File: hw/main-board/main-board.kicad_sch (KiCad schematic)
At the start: 12 parts, among them J1 USB_C_Receptacle_USB2.0_16P, Q1 AONR21307, U1 HUSB238_xxxDD

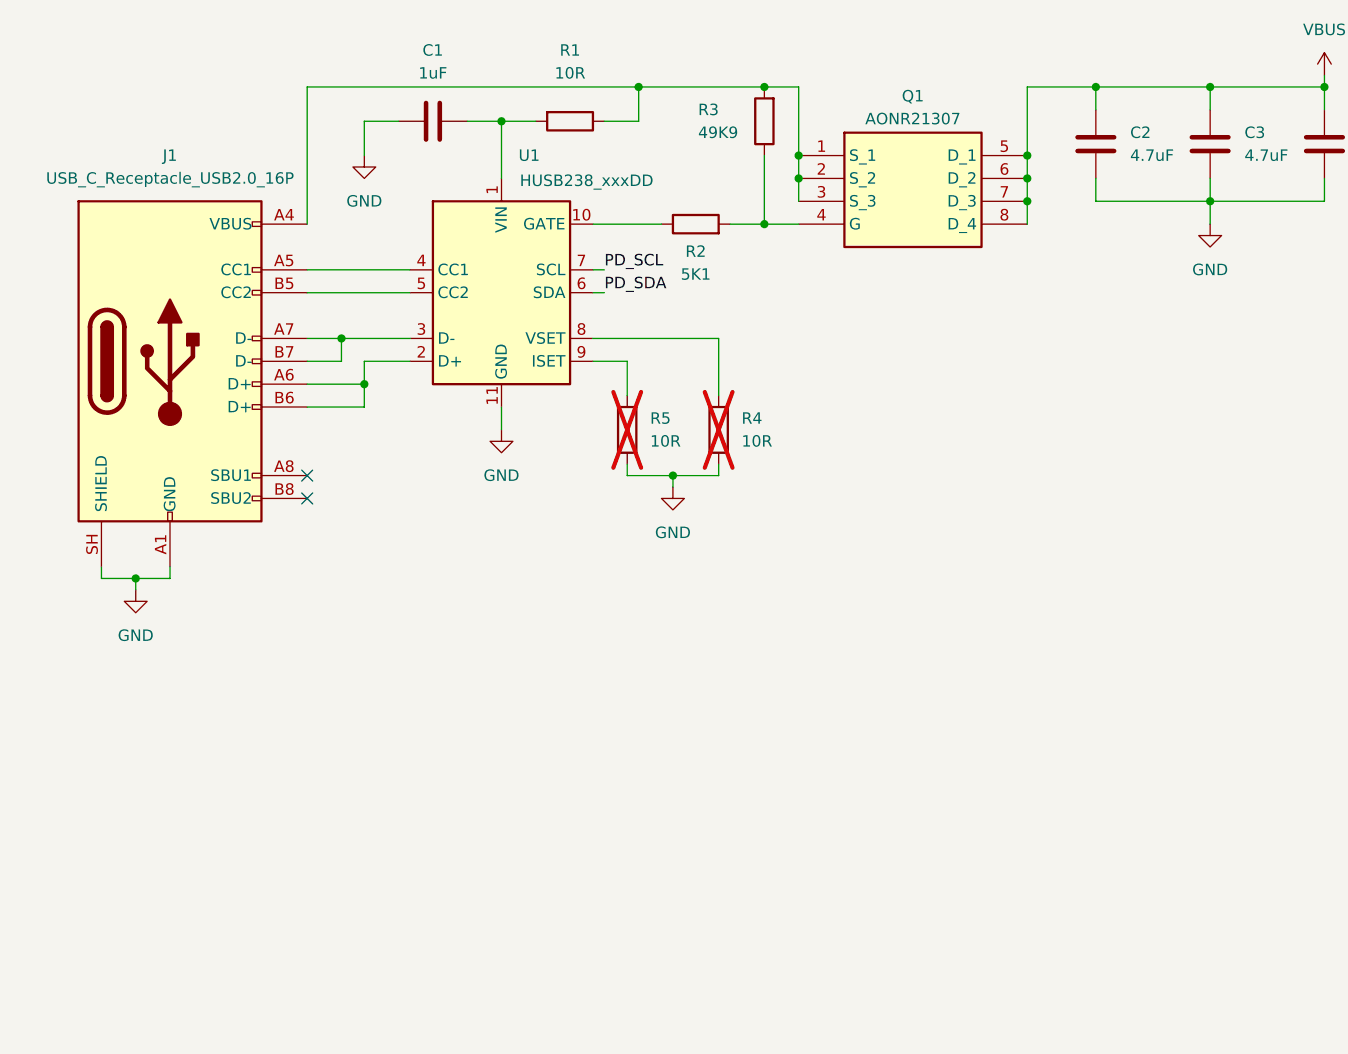
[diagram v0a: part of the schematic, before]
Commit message: Add 5V power schematic and unify components
Adds AP63205WU-based 5V buck converter schematic. Adjusts some
component choices across the board to reduce unique part count.
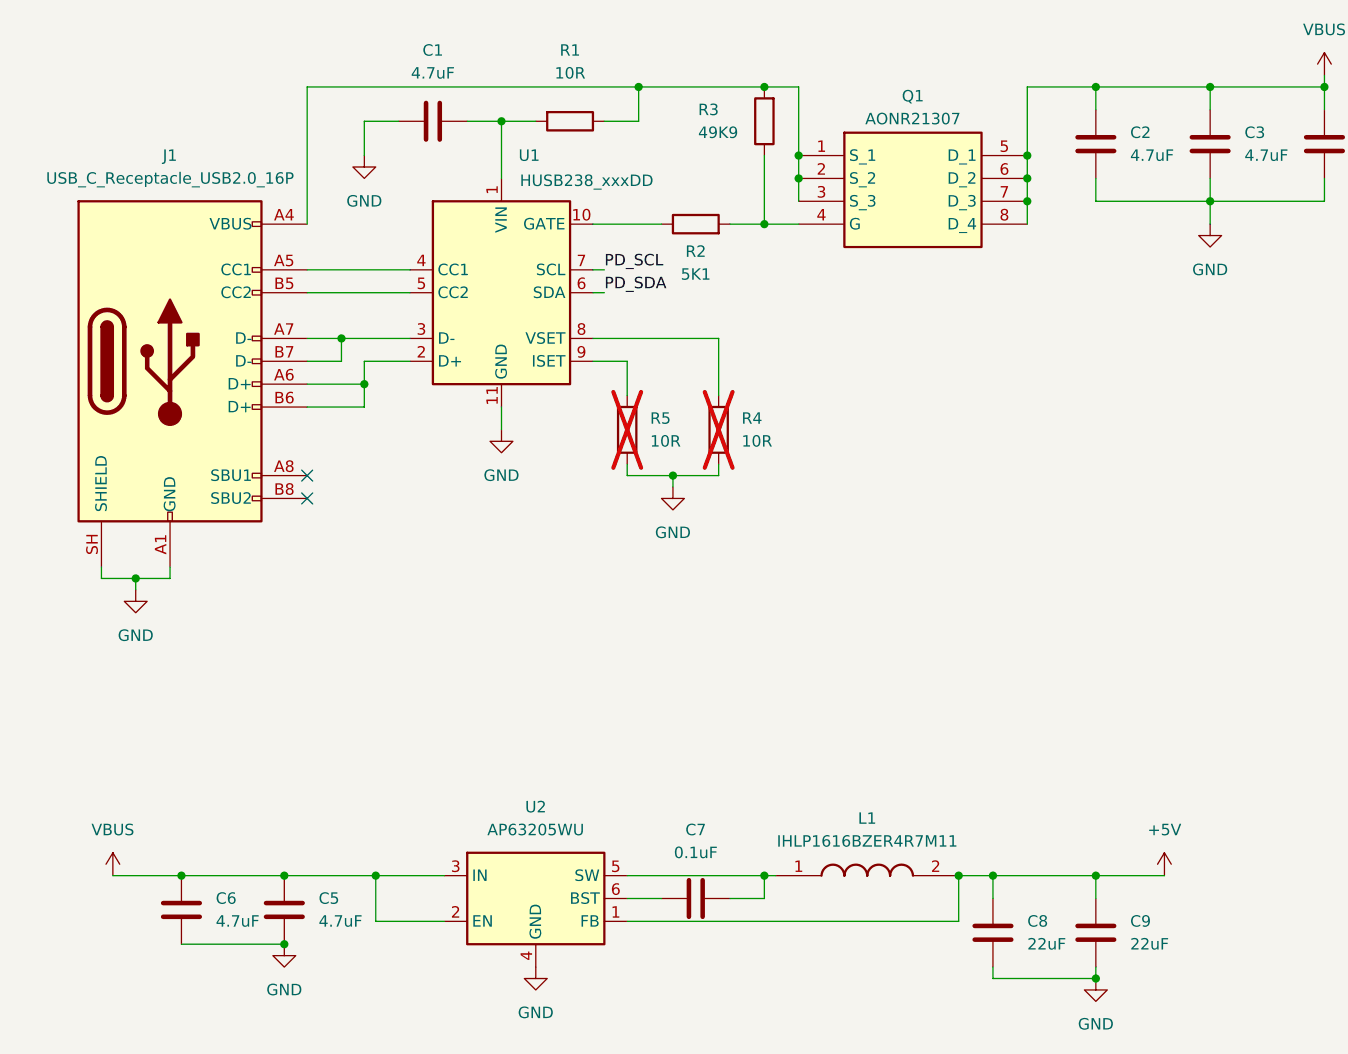
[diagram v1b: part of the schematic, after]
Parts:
- added C5, C6: 4.7uF, Capacitor_SMD:C_0805_2012Metric_Pad1.18x1.45mm_HandSolder, symbol Device:C
- added C7: 0.1uF, Capacitor_SMD:C_0603_1608Metric_Pad1.08x0.95mm_HandSolder, symbol Device:C
- added C8, C9: 22uF, Capacitor_SMD:C_0603_1608Metric_Pad1.08x0.95mm_HandSolder, symbol Device:C
- added L1: IHLP1616BZER4R7M11, INDPM4441X200N, symbol Samacsys:IHLP1616BZER4R7M11
- added U2: AP63205WU, Package_TO_SOT_SMD:TSOT-23-6_HandSoldering, symbol Regulator_Switching:AP63205WU
- C1: value 1uF -> 4.7uF
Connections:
- net GND: now also C5.2, C6.2, C8.1, C9.1, U2.4 (GND)
- net VBUS: now also C5.1, C6.1, U2.2 (EN), U2.3 (IN)
- new net: C7.2, L1.1, U2.5 (SW)
- new net: C7.1, U2.6 (BST)
- new net +5V: C8.2, C9.2, L1.2, U2.1 (FB)

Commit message: Fix SamacSys library links and correct J1 footprint
sym-lib-table pointed at the lib directory instead of the .kicad_sym
file, and there was no project fp-lib-table at all, so the SamacSys
footprints for L1/Q1 could not be resolved. Also J1 was using a
16-pin USB-C symbol paired with a 6-pin footprint that didn't have
matching pads; switched to the Palconn UTC16-G footprint, which
matches all 16 symbol pins.
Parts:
- J1: footprint Package_DFN_QFN:WDFN-10-1EP_3x3mm_P0.5mm_EP1.8x2.5mm -> Connector_USB:USB_C_Receptacle_Palconn_UTC16-G
- L1: footprint INDPM4441X200N -> Samacsys:INDPM4441X200N
- Q1: footprint DFN_3X3_EP -> Samacsys:DFN_3X3_EP
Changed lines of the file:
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@@
 			)
 		)
-		(property "Footprint" "INDPM4441X200N"
+		(property "Footprint" "Samacsys:INDPM4441X200N"
 			(at 125.73 211.76 0)
 			(hide yes)
@@
 			)
 		)
-		(property "Footprint" "Package_DFN_QFN:WDFN-10-1EP_3x3mm_P0.5mm_EP1.8x2.5mm"
+		(property "Footprint" "Connector_USB:USB_C_Receptacle_Palconn_UTC16-G"
 			(at 45.72 58.42 0)
 			(hide yes)
@@
 			)
 		)
-		(property "Footprint" "DFN_3X3_EP"
+		(property "Footprint" "Samacsys:DFN_3X3_EP"
 			(at 133.35 130.48 0)
 			(hide yes)

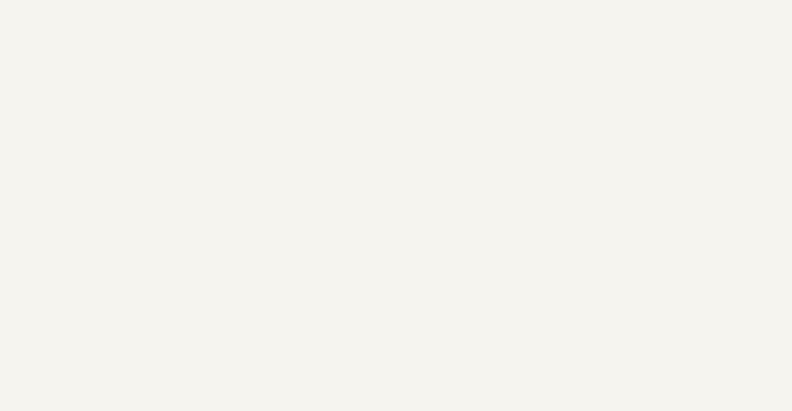
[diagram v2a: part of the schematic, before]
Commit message: Add 3.3V LDO regulator schematic (AP2112K-3.3)
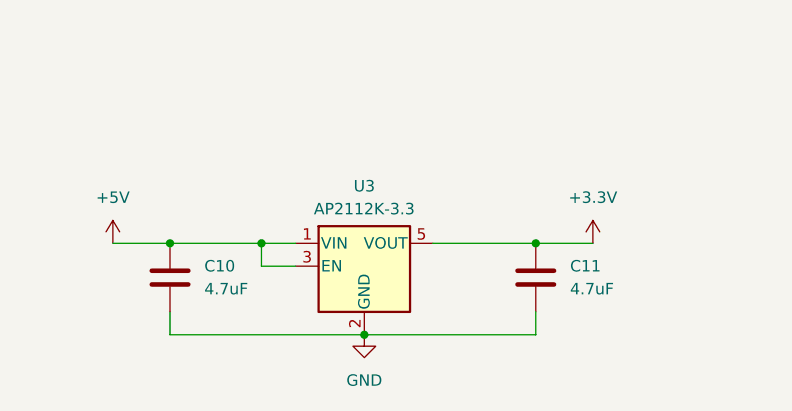
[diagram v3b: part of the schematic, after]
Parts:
- added C10, C11: 4.7uF, Capacitor_SMD:C_0603_1608Metric_Pad1.08x0.95mm_HandSolder, symbol Device:C
- added U3: AP2112K-3.3, Package_TO_SOT_SMD:SOT-23-5, symbol Regulator_Linear:AP2112K-3.3
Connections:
- net +5V: now also C10.1, U3.1 (VIN), U3.3 (EN)
- net GND: now also C10.2, C11.2, U3.2 (GND)
- new net +3.3V: C11.1, U3.5 (VOUT)

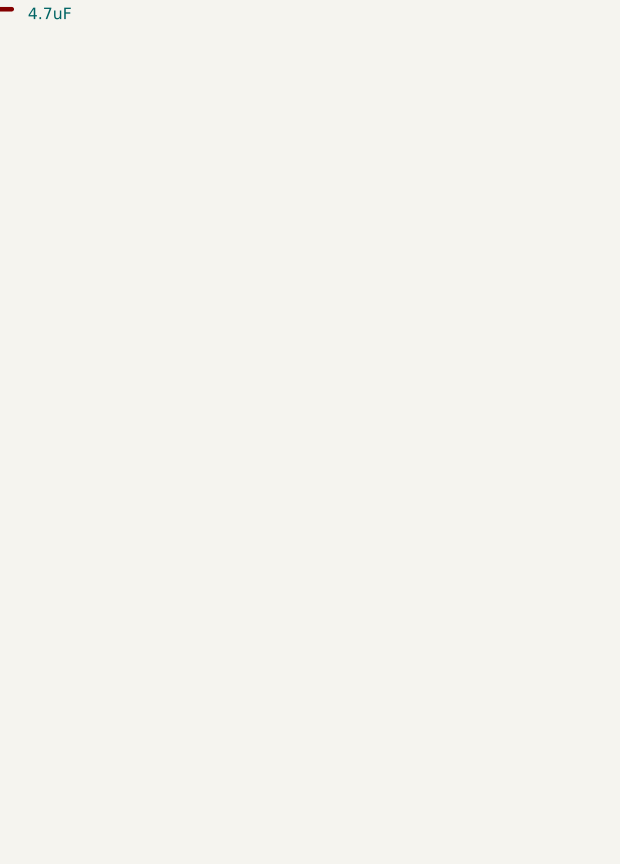
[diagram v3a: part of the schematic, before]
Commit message: Add PTR54L connector schematic with project-specific symbol and footprint library
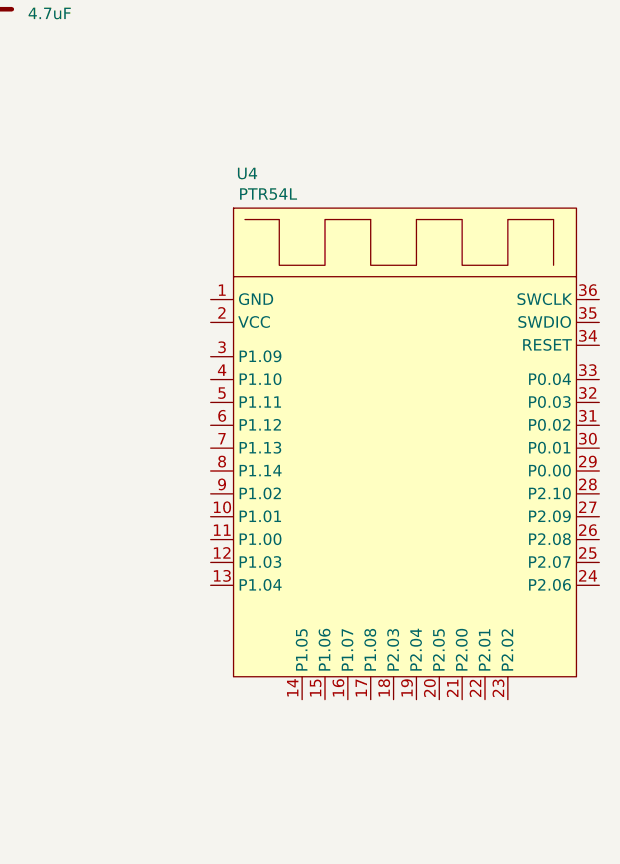
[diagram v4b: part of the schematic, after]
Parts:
- added U4: PTR54L, Project_Specific_Parts:PTR54L15, symbol Project_Specific_Parts:PTR54L
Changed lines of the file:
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@@
+	)
+	(symbol
+		(lib_id "Project_Specific_Parts:PTR54L")
+		(at 196.85 64.77 0)
+		(unit 1)
+		(body_style 1)
+		(exclude_from_sim no)
+		(in_bom yes)
+		(on_board yes)
+		(in_pos_files yes)
+		(dnp no)
+		(fields_autoplaced yes)
+		(property "Reference" "U4"
+			(at 198.374 53.34 0)
+			(show_name no)
+			(do_not_autoplace no)
+			(effects
+				(font
+					(size 1.27 1.27)
+				)
+			)
+		)
+		(property "Value" "PTR54L"
+			(at 200.66 55.626 0)
+			(show_name no)
+			(do_not_autoplace no)
+			(effects
+				(font
+					(size 1.27 1.27)
+				)
+			)
+		)
+		(property "Footprint" "Project_Specific_Parts:PTR54L15"
+			(at 196.85 64.77 0)
+			(hide yes)
+			(show_name no)
+			(do_not_autoplace no)
+			(effects
+				(font
+					(size 1.27 1.27)
+				)
+			)
+		)
+		(property "Datasheet" ""
+			(at 196.85 64.77 0)
+			(hide yes)
+			(show_name no)
+			(do_not_autoplace no)
+			(effects
+				(font
+					(size 1.27 1.27)
+				)
+			)
+		)
+		(property "Description" ""
+			(at 196.85 64.77 0)
+			(hide yes)
+			(show_name no)
+			(do_not_autoplace no)
+			(effects
+				(font
+					(size 1.27 1.27)
+				)
+			)
+		)
+		(pin "5"
+		)
+		(pin "7"
+		)
+		(pin "1"
+		)
+		(pin "14"
+		)
+		(pin "10"
+		)
+		(pin "4"
+		)
+		(pin "3"
+		)
+		(pin "11"
+		)
+		(pin "13"
+		)
+		(pin "2"
+		)
+		(pin "8"
+		)
+		(pin "9"
+		)
+		(pin "6"
+		)
+		(pin "15"
+		)
+		(pin "12"
+		)
+		(pin "33"
+		)
+		(pin "27"
+		)
+		(pin "26"
+		)
+		(pin "36"
+		)
+		(pin "35"
+		)
+		(pin "32"
+		)
+		(pin "24"
+		)
+		(pin "30"
+		)
+		(pin "17"
+		)
+		(pin "22"
+		)
+		(pin "29"
+		)
+		(pin "34"
+		)
+		(pin "18"
+		)
+		(pin "19"
+		)
+		(pin "21"
+		)
+		(pin "16"
+		)
+		(pin "23"
+		)
+		(pin "28"
+		)
+		(pin "25"
+		)
+		(pin "20"
+		)
+		(pin "31"
+		)
+		(instances
+			(project "main-board"
+				(path "/fe215afa-a228-4dbb-8560-a0753323a3f2"
+					(reference "U4")
+					(unit 1)
+				)
+			)
+		)
 	)
 	(symbol

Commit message: Add PTR54L power circuit and initial PCB outline with placed components
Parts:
- added C12: 100nF, Capacitor_SMD:C_0603_1608Metric_Pad1.08x0.95mm_HandSolder, symbol Device:C
- added C13: 22uF, Capacitor_SMD:C_0603_1608Metric_Pad1.08x0.95mm_HandSolder, symbol Device:C
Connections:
- net +3.3V: now also U4.2 (VCC), C12.2, C13.2
- net GND: now also U4.1 (GND), C12.1, C13.1

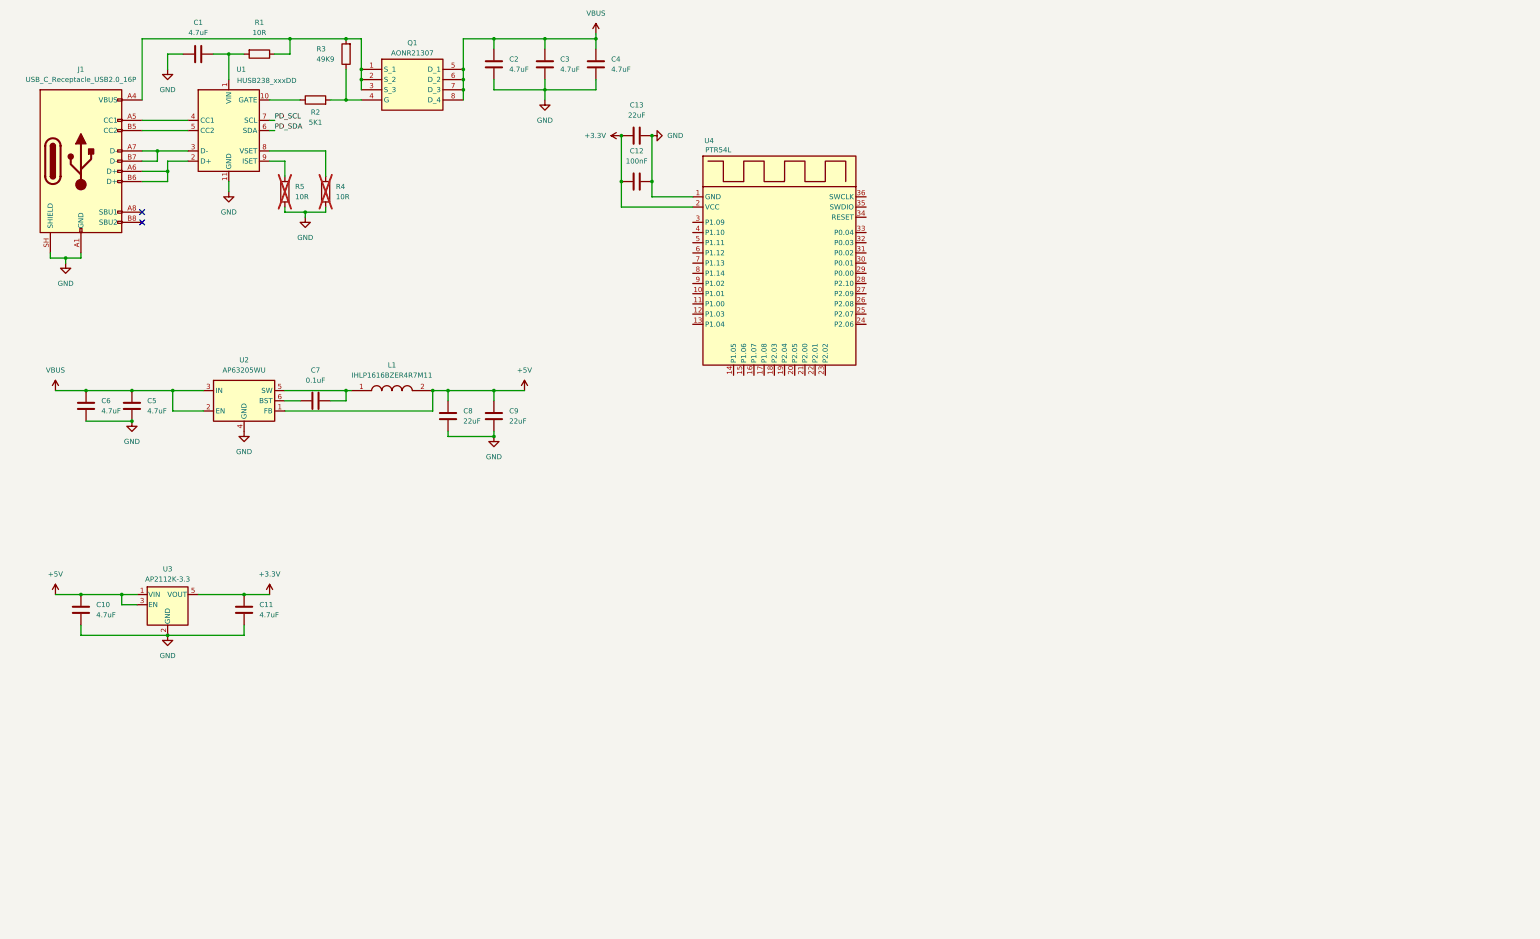
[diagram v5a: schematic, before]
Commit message: Fix capacitor value, switch schematic sheet to A3, add TMC2226 driver symbol
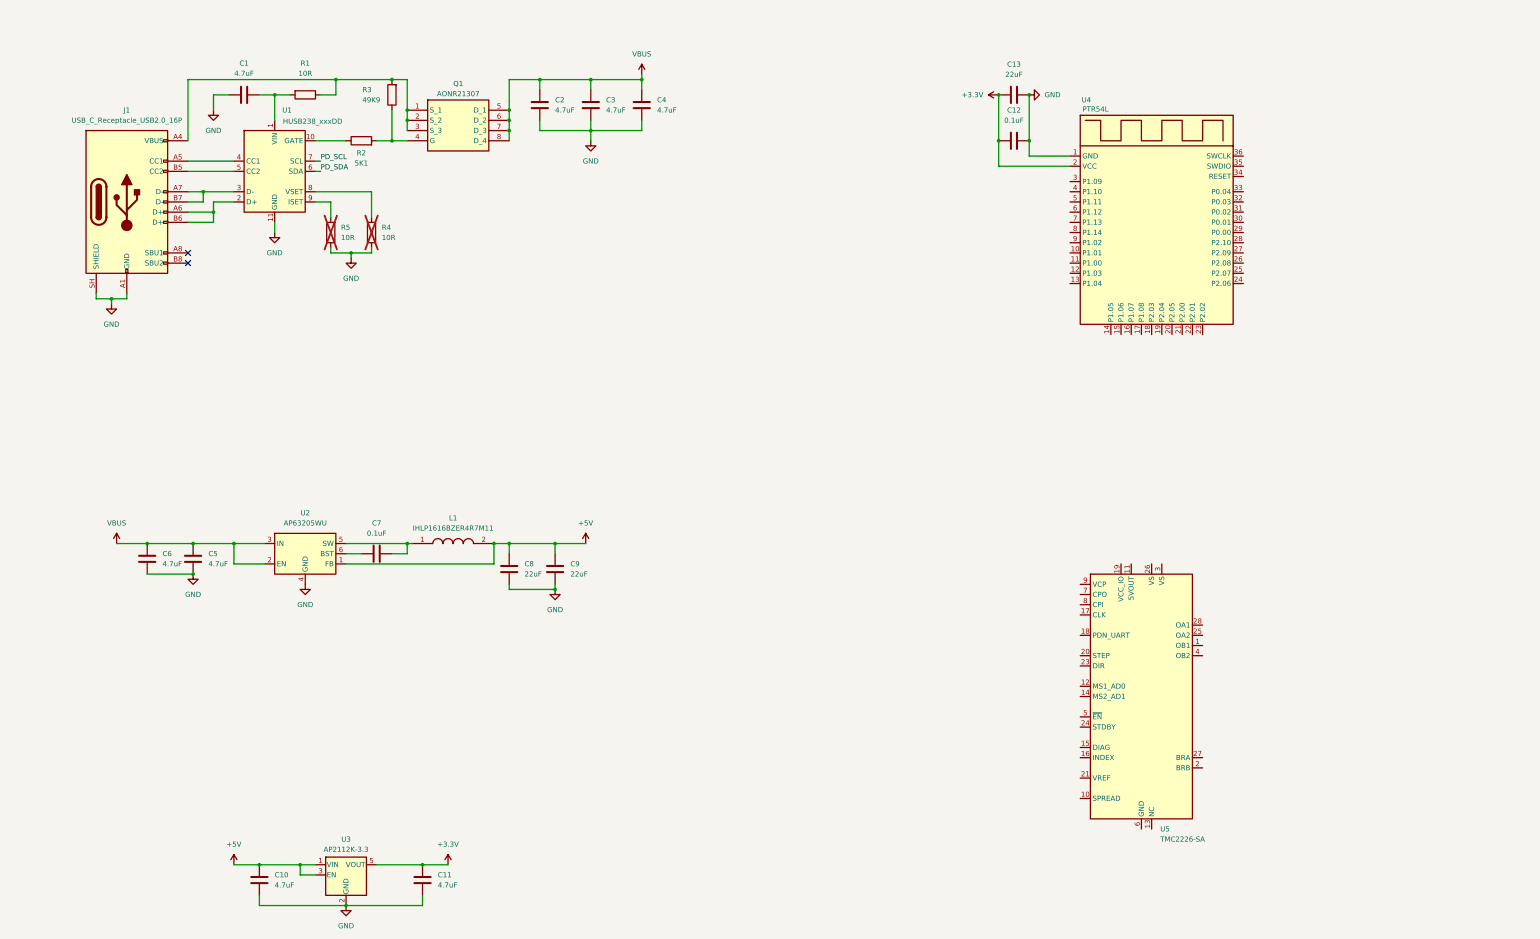
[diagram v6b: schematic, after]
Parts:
- added U5: TMC2226-SA, Package_SO:HTSSOP-28-1EP_4.4x9.7mm_P0.65mm_EP2.75x6.2mm_ThermalVias, symbol Driver_Motor:TMC2226-SA
- C12: value 100nF -> 0.1uF
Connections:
- new net: U5.22 (GND), U5.29 (GND), U5.6 (GND)
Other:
- moved on the sheet: C1, C10, C11, C12, C13, C2, C3, C4, C5, C6, C7, C8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

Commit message: Add 3d model for WDFN10 component, change footprint for 5V buck converter
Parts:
- U2: footprint Package_TO_SOT_SMD:TSOT-23-6_HandSoldering -> Package_TO_SOT_SMD:TSOT-23-6
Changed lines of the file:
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@@
 			)
 		)
-		(property "Footprint" "Package_TO_SOT_SMD:TSOT-23-6_HandSoldering"
+		(property "Footprint" "Package_TO_SOT_SMD:TSOT-23-6"
 			(at 97.79 179.07 0)
 			(hide yes)
